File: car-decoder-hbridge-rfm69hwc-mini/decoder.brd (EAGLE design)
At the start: 96.5 x 80 mm, 50 parts, among them U1 RFM69HCW, U2 ATMEGA328P-MU, U3 MCP73831, U6 MIC5219 3.3V, Y1 16MHZ

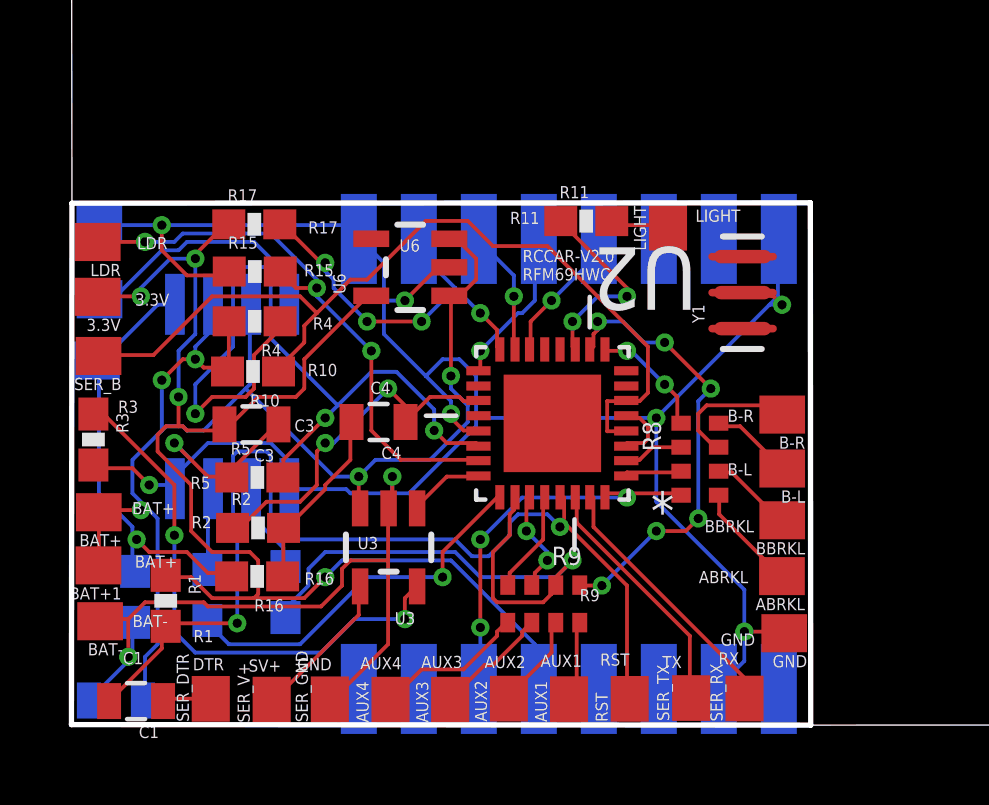
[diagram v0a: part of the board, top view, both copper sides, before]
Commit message: Fix boards and add the pi control station
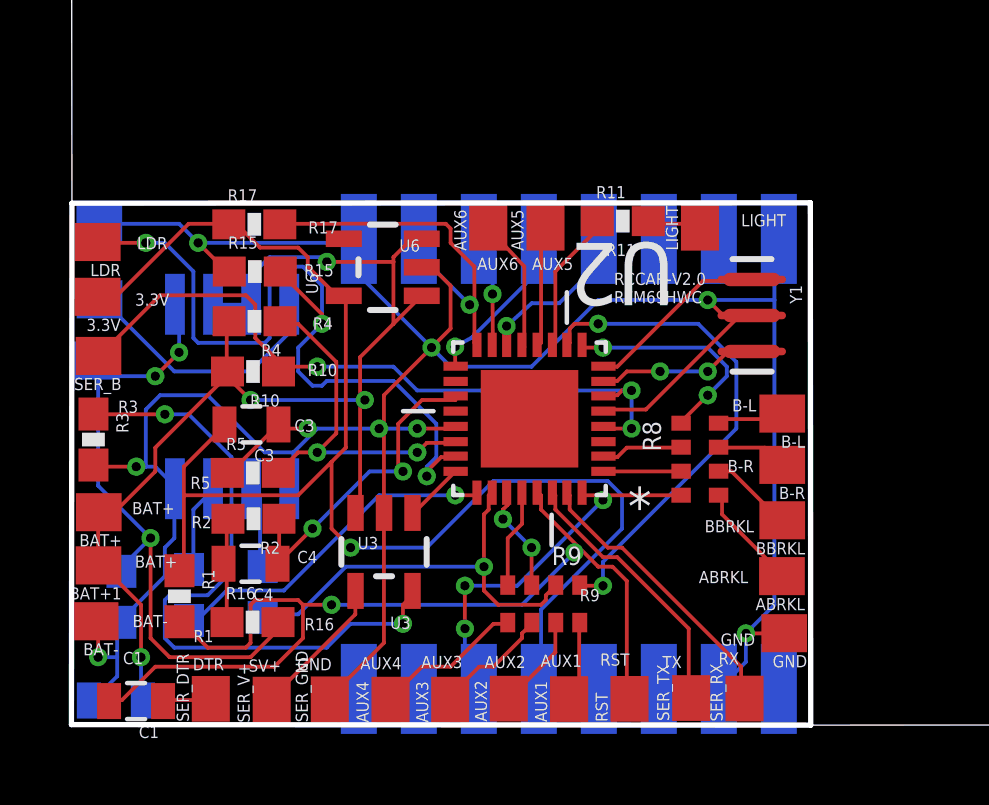
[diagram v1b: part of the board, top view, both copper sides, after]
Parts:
- added AUX5, AUX6: (no value), wirepad:SMD1,27-2,54
- moved C4 6.37 mm to (9.52, 5.34)
- moved B-L 1.83 mm to (27.2, 10.3)
- moved B-R 1.68 mm to (27.2, 8.63)
- moved R16 1.53 mm to (9.59, 3.39), turned to 0 degrees
- moved R11 1.22 mm to (21.9, 16.8)
- moved LIGHT 1.07 mm to (24.5, 16.5)
- moved U6 0.91 mm to (13.9, 15.2)
- moved Y1 0.82 mm to (26.2, 13.6), turned to 270 degrees
- moved U2 0.78 mm to (18.8, 10.2)
- moved R6 0.76 mm to (9.93, 4.39)
- moved R7 0.61 mm to (7.47, 4.30)
- moved R1 0.48 mm to (7.15, 4.25)
- moved R14 0.46 mm to (5.22, 4.23)
- moved R2 0.34 mm to (9.62, 6.84), turned to 180 degrees
- moved R5 0.22 mm to (9.60, 8.37)
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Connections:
- new net D8: AUX5.1, U2.12
- new net D9: AUX6.1, U2.13
- net GND: no longer U2.3
- net N$2: now also Y1.1
- net N$4: now also Y1.3
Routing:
- net A7: track 26.7 -> 12.1 mm, vias 3 -> 2
- net A0: track 19.3 -> 27.0 mm
- net OA: track 14.7 -> 21.9 mm, vias 1 -> 3
- net BAT+: track 45.8 -> 40.2 mm, vias 5 -> 4
- net N$4: track 0.00 -> 5.34 mm, vias 0 -> 2
- net N$2: track 0.00 -> 5.19 mm
- net N$8: track 29.5 -> 24.5 mm, vias 0 -> 3
- net D9: track 0.00 -> 4.58 mm
- net A3: track 19.0 -> 14.4 mm
- net N$11: track 18.3 -> 22.5 mm
- net D8: track 0.00 -> 4.11 mm
- net BL: track 4.04 -> 7.64 mm
- net VCC: track 44.7 -> 48.1 mm, vias 4 -> 1
- net GND: track 103.5 -> 100.4 mm, vias 10 -> 9
- net N$1: track 6.15 -> 3.59 mm
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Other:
- board text added: "AUX5"
- board text added: "AUX6"
